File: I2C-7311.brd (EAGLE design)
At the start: 106 x 100 mm, 47 parts, among them IC1 MAX7311, J1 CONNECTOR-I2CLEFT, J2 CONNECTOR-I2CLEFT, J5 CONNECTOR-GROVE-4P-2.0-347013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, J8 CONNECTOR-GROVE-4P-2.0-347013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, SW1 A0, SW2 A1, SW3 A2

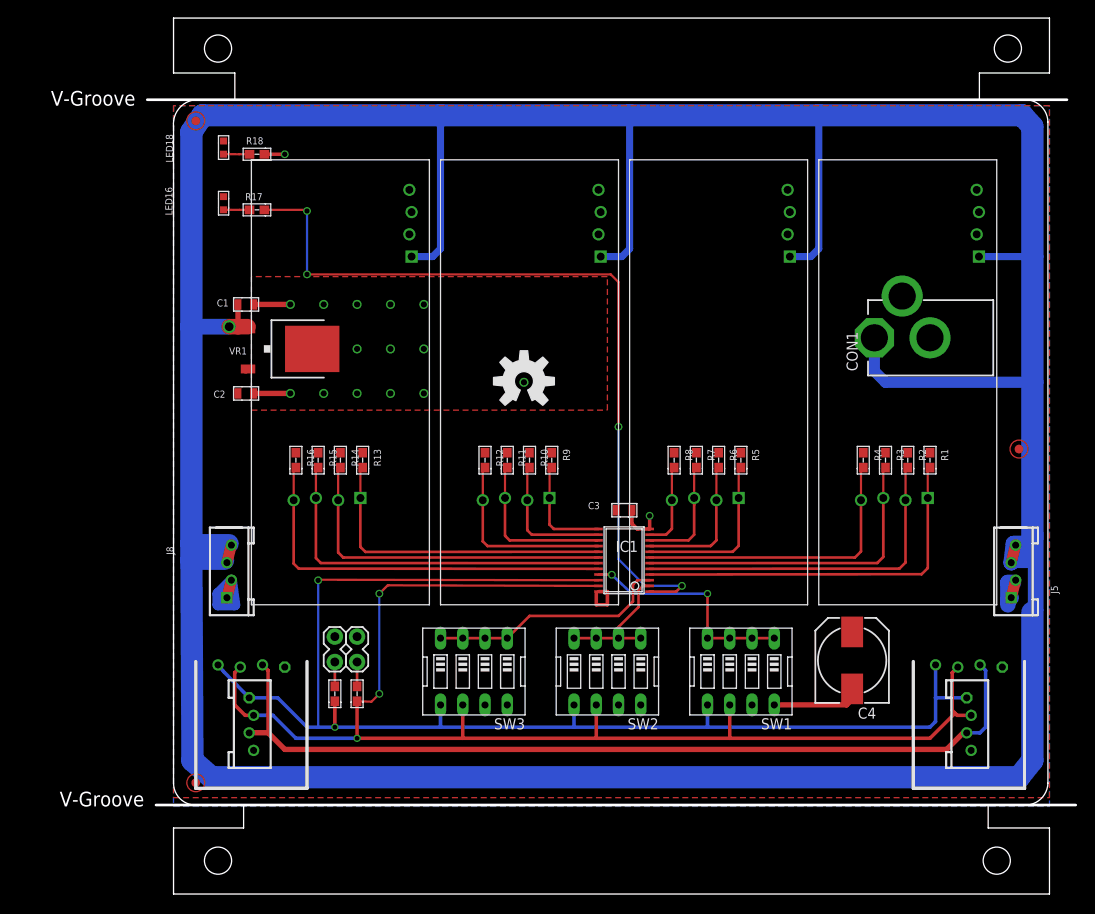
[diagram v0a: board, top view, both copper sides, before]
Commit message: 3.0 - new IOB design
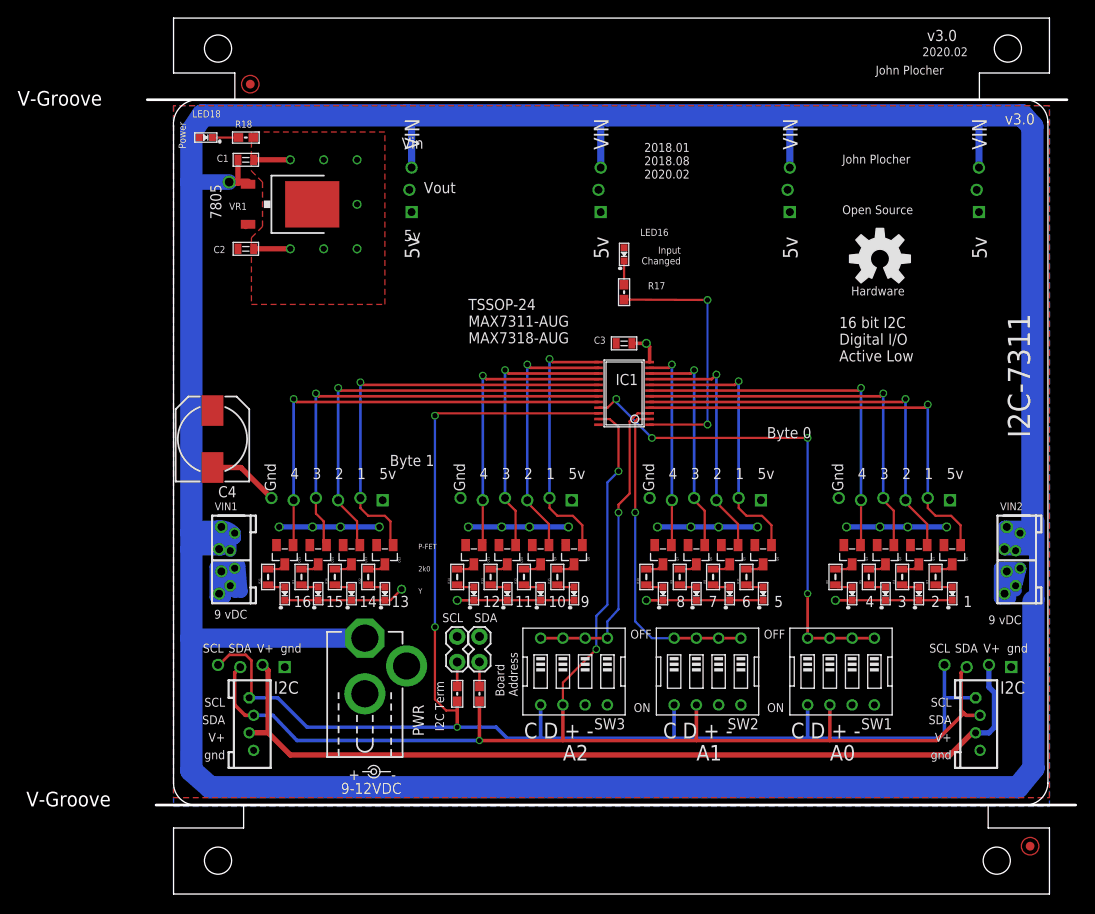
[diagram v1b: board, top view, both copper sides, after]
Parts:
- removed CON1: (no value), SPCoast:DCJ0202
- removed FID3: FIDUCIAL, SPCoast:FIDUCIAL_1MM
- removed J5, J8: CONNECTOR-GROVE-4P-2.0-3470130P1, SPCoast:4P-2.0
- removed R2, R3: 10k, SPCoast:0603-RES
- added LED1, LED10, LED11, LED12, LED13, LED14, LED15, LED17, LED2, LED3, LED4, LED5, LED6, LED7, LED8, LED9: Y, SPCoast:0603-LED
- added PWR: (no value), SPCoast:DCJ0202
- added Q0, Q1, Q10, Q11, Q12, Q13, Q14, Q15, Q2, Q3, Q4, Q5, Q6, Q7, Q8, Q9: P-FET, SPCoast:SOT23
- added R21, R22: 2K0, SPCoast:0805-RES
- added VIN: 9-12VDC, SPCoast:PWR_LABEL
- added VIN1, VIN2: CONNECTOR-POWER-L, SPCoast:POWER-R2
- BOARD1: value (none) -> BOARD80X100-IOB; device SPCoast:BOARD-DINRAIL-3.17IN-NOHOLES -> SPCoast:BOARD-DINRAIL-3.17IN-IOB
- IOB1, IOB2, IOB3, IOB4: value IO4-IOBBARE -> CONNECTOR-IO4-IOBBARE
- J1, J2: value CONNECTOR-I2CLEFT -> (none)
- R1, R10, R11, R12, R13, R14, R15, R16, R4, R5, R6, R7, R8, R9: value 10k -> 2K0; device SPCoast:0603-RES -> SPCoast:0805-RES
- SW1, SW2, SW3: device special:EDG-04 -> SPCoast:EDG-04
- moved FID2 95.5 mm to (97.8, 5.46)
- moved C4 77.3 mm to (4.45, 51.9)
- moved R1 73.0 mm to (14.6, 36.2), turned to 90 degrees
- moved LED16 46.1 mm to (51.4, 73.0)
- moved U$1 43.0 mm to (80.6, 72.5)
- moved R17 43.0 mm to (51.4, 68.7), turned to 270 degrees
- moved R7 30.4 mm to (87.0, 36.2), turned to 90 degrees
- moved R15 30.4 mm to (43.8, 36.2), turned to 90 degrees
- moved R11 30.4 mm to (65.4, 36.2), turned to 90 degrees
- moved R13 19.8 mm to (36.2, 36.2), turned to 90 degrees
- moved R5 19.8 mm to (79.4, 36.2), turned to 90 degrees
- moved R9 19.8 mm to (57.8, 36.2), turned to 90 degrees
- moved C3 19.1 mm to (51.4, 62.9)
- moved IC1 19.0 mm to (51.4, 57.1)
- moved R10 18.9 mm to (54.0, 36.2), turned to 90 degrees
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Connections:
- new net N$10: Q8.3, R15.2
- new net N$11: Q9.3, R12.2
- new net N$12: Q10.3, R13.2
- new net N$13: Q11.3, R14.2
- new net N$14: LED12.A, R15.1
- new net N$15: LED9.A, R12.1
- new net N$2: Q4.3, R11.2
- new net N$23: LED10.A, R13.1
- new net N$24: LED11.A, R14.1
- new net N$28: Q12.3, R22.2
- new net N$29: Q13.3, R16.2
- new net N$3: Q5.3, R8.2
- new net N$30: Q14.3, R1.2
- new net N$31: Q15.3, R21.2
- new net N$32: LED17.A, R22.1
- new net N$33: LED13.A, R16.1
- new net N$34: LED14.A, R1.1
- new net N$35: LED15.A, R21.1
- new net N$4: Q6.3, R9.2
- new net N$44: Q0.3, R7.2
- new net N$45: Q1.3, R4.2
- new net N$46: Q2.3, R5.2
- new net N$47: Q3.3, R6.2
- new net N$48: LED1.A, R7.1
- new net N$49: LED2.A, R4.1
- new net N$5: Q7.3, R10.2
- new net N$50: LED3.A, R5.1
- new net N$51: LED4.A, R6.1
- new net N$6: LED8.A, R11.1
- new net N$7: LED5.A, R8.1
- new net N$8: LED6.A, R9.1
- new net N$9: LED7.A, R10.1
- net +9V: now also PWR.1, VIN1.V+, VIN1.V+@1, VIN1.V+@2, VIN1.V+@3, VIN2.V+, VIN2.V+@1, VIN2.V+@2, VIN2.V+@3; no longer CON1.1, J5.3, J5.4, J8.3, J8.4
- net GND: now also IOB1.G@3, IOB2.G@3, IOB3.G@3, IOB4.G@3, LED1.C, LED10.C, LED11.C, LED12.C, LED13.C, LED14.C, LED15.C, LED17.C, LED2.C, LED3.C, LED4.C, LED5.C, LED6.C, LED7.C, LED8.C, LED9.C, PWR.2, PWR.3, VIN1.GND, VIN1.GND@1, VIN1.GND@2, VIN1.GND@3, VIN2.GND, VIN2.GND@1, VIN2.GND@2, VIN2.GND@3; no longer CON1.2, CON1.3, IOB1.G@1, IOB1.G@2, IOB2.G@1, IOB2.G@2, IOB3.G@1, IOB3.G@2, IOB4.G@1, IOB4.G@2, J5.1, J5.2, J8.1, J8.2
- net P1: now also Q0.1; no longer R1.2
- net P10: now also Q9.1; no longer R10.2
- net P11: now also Q10.1; no longer R11.2
- net P12: now also Q11.1; no longer R12.2
- net P13: now also Q12.1; no longer R13.2
- net P14: now also Q13.1; no longer R14.2
- net P15: now also Q14.1; no longer R15.2
- net P16: now also Q15.1; no longer R16.2
- net P2: now also Q1.1; no longer R2.2
- net P3: now also Q2.1; no longer R3.2
- net P4: now also Q3.1; no longer R4.2
- net P5: now also Q4.1; no longer R5.2
- net P6: now also Q5.1; no longer R6.2
- net P7: now also Q6.1; no longer R7.2
- net P8: now also Q7.1; no longer R8.2
- net P9: now also Q8.1; no longer R9.2
- net VCC: now also IOB1.V5@1, IOB2.V5@1, IOB3.V5@1, IOB4.V5@1, Q0.2, Q1.2, Q10.2, Q11.2, Q12.2, Q13.2, Q14.2, Q15.2, Q2.2, Q3.2, Q4.2, Q5.2, Q6.2, Q7.2, Q8.2, Q9.2; no longer R1.1, R10.1, R11.1, R12.1, R13.1, R14.1, R15.1, R16.1, R2.1, R3.1, R4.1, R5.1, R6.1, R7.1, R8.1, R9.1
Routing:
- net GND: track 42.1 -> 112.2 mm, vias 16 -> 12
- net !INT: track 92.2 -> 30.4 mm, vias 4 -> 2
- net VCC: track 5.42 -> 50.9 mm, vias 0 -> 16
- net A0: track 26.0 -> 56.8 mm, vias 2 -> 4
- net A1: track 15.5 -> 37.9 mm, vias 0 -> 1
- net +9V: track 455.8 -> 436.4 mm
- net P9: track 12.4 -> 29.6 mm, vias 0 -> 1
- net SCL: track 154.6 -> 170.5 mm, vias 2 -> 3
- net P10: track 15.6 -> 29.9 mm, vias 0 -> 1
- net P8: track 9.90 -> 23.6 mm, vias 0 -> 1
- net P11: track 18.8 -> 31.3 mm, vias 0 -> 1
- net P5: track 19.5 -> 31.6 mm, vias 0 -> 1
- net P7: track 13.9 -> 25.7 mm, vias 0 -> 1
- net P6: track 16.8 -> 28.3 mm, vias 0 -> 1
- net P13: track 36.6 -> 48.1 mm, vias 0 -> 1
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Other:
- board text added: "1"
- board text added: "10"
- board text added: "11"
- board text added: "12"
- board text added: "13"
- board text added: "14"
- board text added: "15"
- board text added: "16"
- board text added: "2"
- board text added: "2018.01 2018.08 2020.02"
- board text added: "2020.02"
- board text added: "2k0"
- board text added: "3"
- board text added: "3.0 - new IOB footprint"
- board text added: "4"
- board text added: "5"
- board text added: "6"
- board text added: "7"
- board text added: "8"
- board text added: "9"
- board text added: "OFF"
- board text added: "ON"
- board text added: "P-FET"
- board text added: "TSSOP-24 MAX7311-AUG MAX7318-AUG"
- board text added: "Vout"
- board text added: "Y"
- board text added: "v3.0"
- board text removed: "10k pullups for use with MAX7312"
- board text removed: "2018.01 2018.08"
- board text removed: "2018.08"
- board text removed: "4 3 2 1"
- board text removed: "8 7 6 5"
- board text removed: "External daughterboards for each IO bank Eliminates having to custom cut 3M track Eliminates having to stock signal driver I2C boards Custom input low pass filters can be added to Detector and Turtle drivers 2.0 - fixed footprint for U1, DB keepout violations 2.1 - Added carrier template, optional DC barrel power jack"
- board text removed: "I2C-7311-IO"
- board text removed: "MAX7311 /12 AUG or PCA9675PW"
- board text removed: "gnd"
- board text removed: "v2.1"

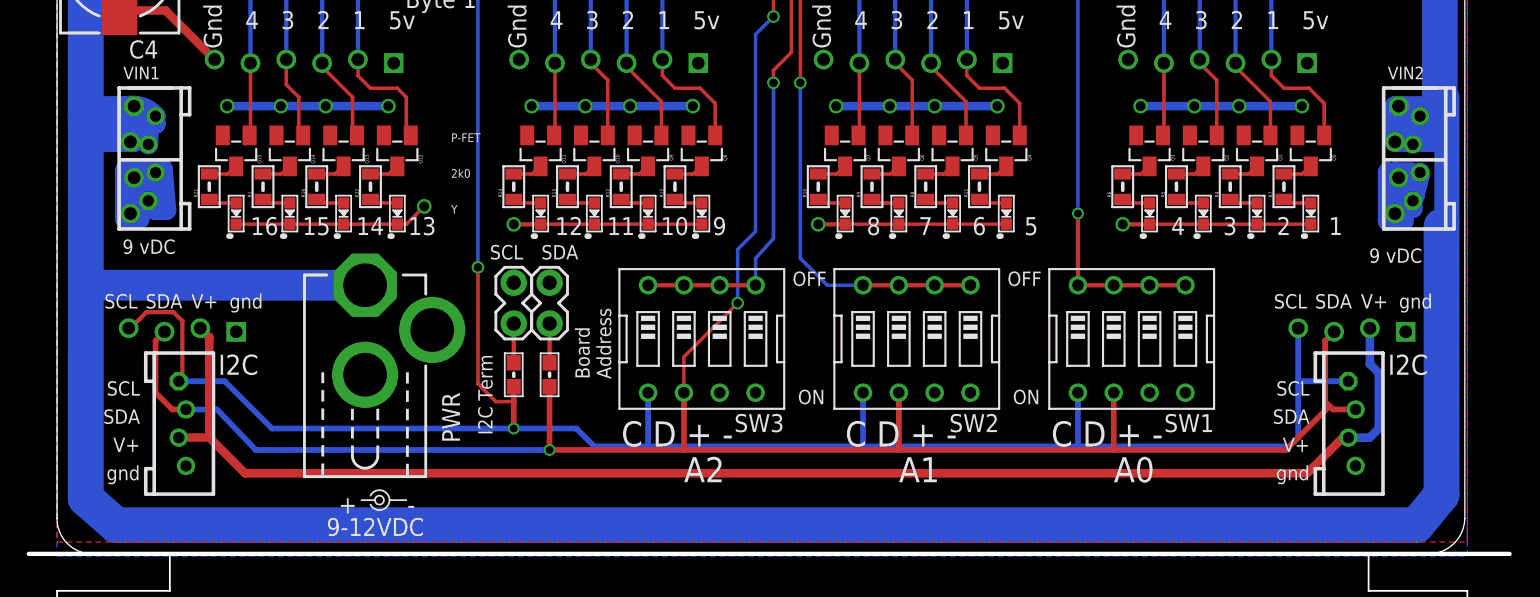
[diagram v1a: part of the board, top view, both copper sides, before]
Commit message: updated SPCoast lib for IO4-IOB silkscreen
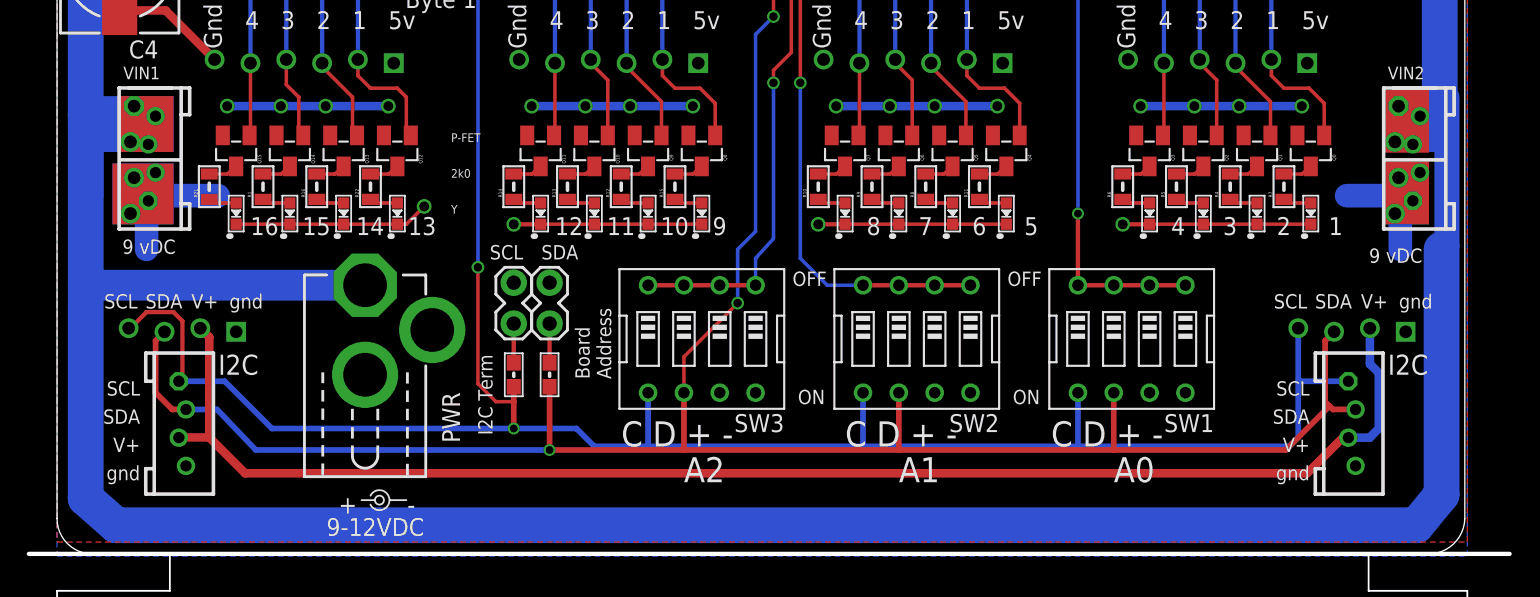
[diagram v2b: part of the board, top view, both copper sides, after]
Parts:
- IOB1, IOB2, IOB3: value CONNECTOR-IO4-IOBBARE -> CONNECTOR-IO4-IOBCLEAN; device SPCoast:IO4-IOB -> SPCoast:IOB-IO4-CLEAN
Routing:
- net GND: track 112.2 -> 100.2 mm
- net +9V: track 436.4 -> 429.3 mm
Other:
- board text removed: "Made in the PCR, Coast Division, NMRA"
- board text removed: "Model Railroading is fun!"

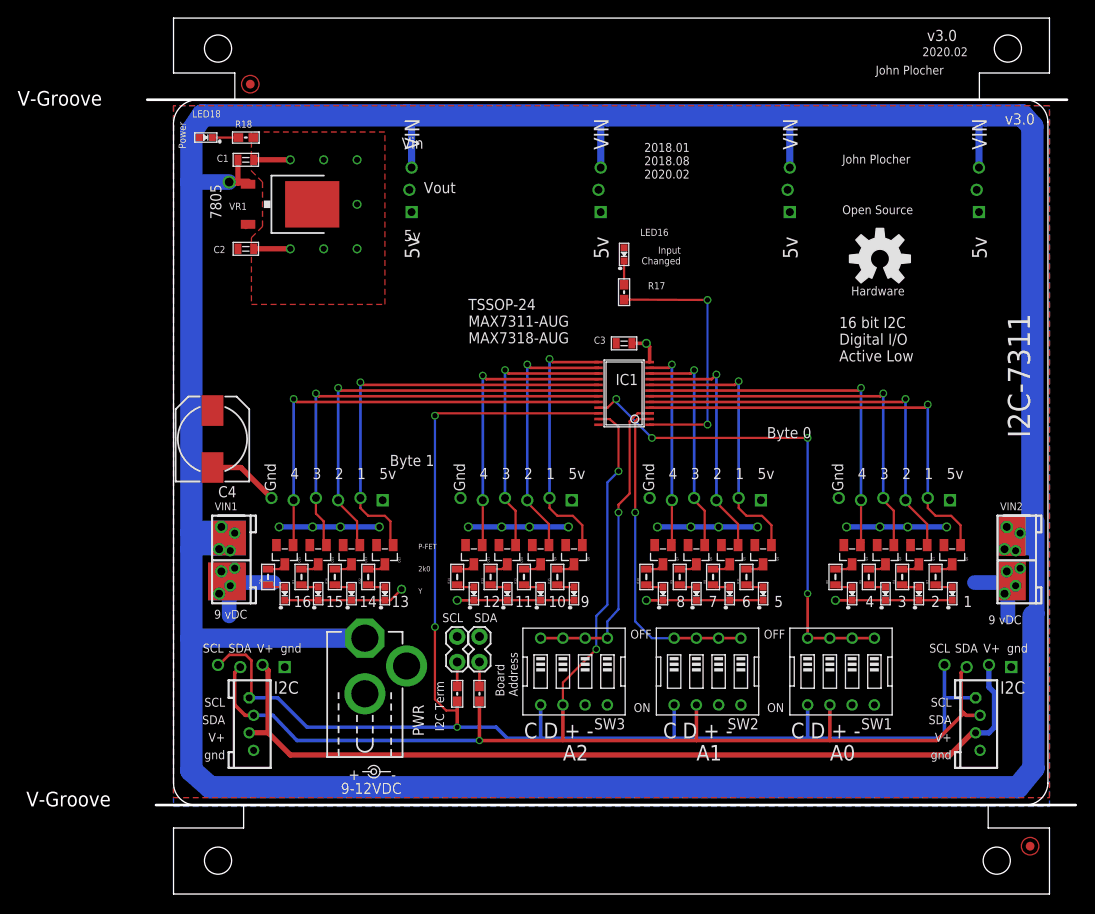
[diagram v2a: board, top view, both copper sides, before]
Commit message: updated SPCoast.lbr: LED, VR, C-POL to match reel orientation
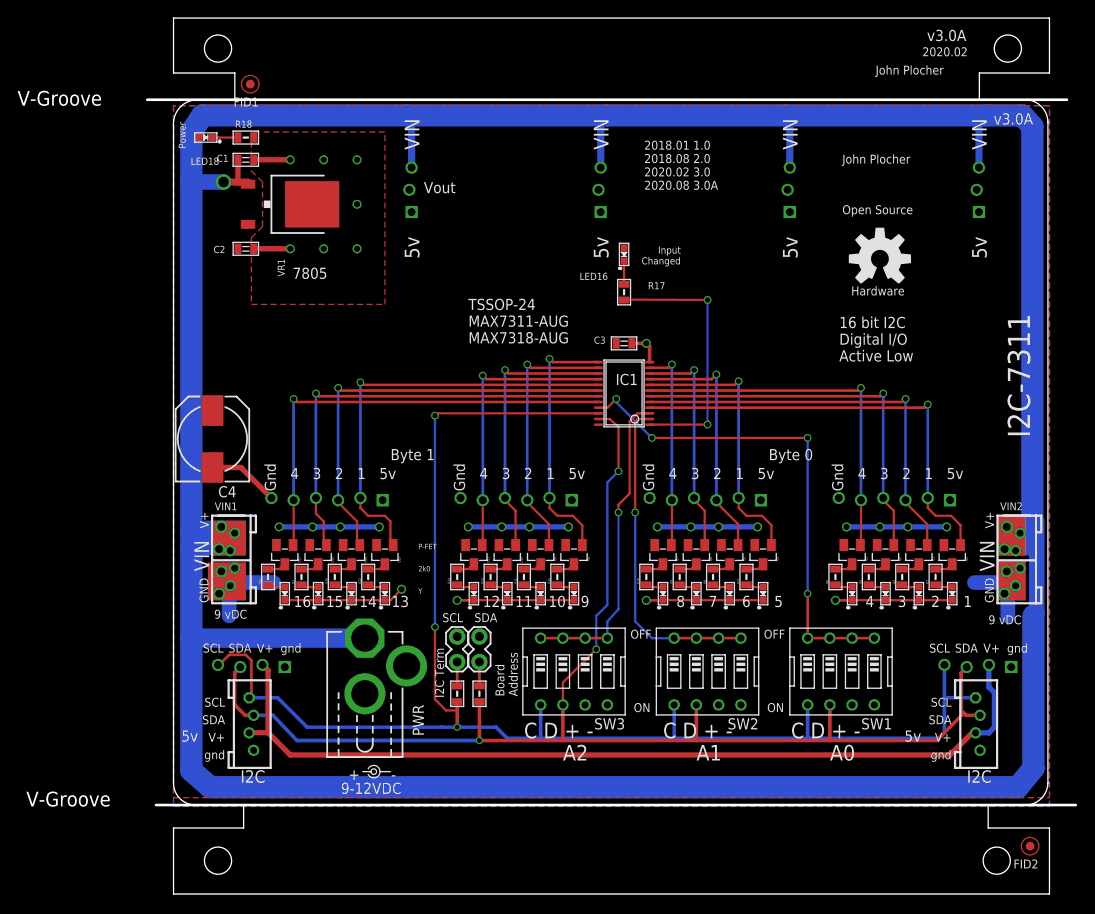
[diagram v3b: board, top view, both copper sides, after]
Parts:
- LED16, LED18: value DIM-GREEN -> G
- R17: value 2k2 -> 2k0; device SPCoast:0603-RES -> SPCoast:0805-RES
- R18: value 2K2 -> 2K0; device SPCoast:0603-RES -> SPCoast:0805-RES
- R19, R20: device SPCoast:0603-RES -> SPCoast:0805-RES
- turned LED1 to 90 degrees
- turned LED10 to 90 degrees
- turned LED11 to 90 degrees
- turned LED12 to 90 degrees
- turned LED13 to 90 degrees
- turned LED14 to 90 degrees
- turned LED15 to 90 degrees
- turned LED16 to 90 degrees
- turned LED17 to 90 degrees
- turned LED18 to 180 degrees
- turned LED2 to 90 degrees
- turned LED3 to 90 degrees
- turned LED4 to 90 degrees
- turned LED5 to 90 degrees
- turned LED6 to 90 degrees
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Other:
- board text added: "2018.01 1.0 2018.08 2.0 2020.02 3.0 2020.08 3.0A"
- board text added: "3.0A - Fixed C-POL, LED and VREG library component orientations to match default reel orientation, no PCB changes"
- board text added: "A "1" bit in the I/O register is associated with a LOW voltage on a pin, and a LIT feedback LED."
- board text added: "v3.0A"
- board text removed: "2018.01 2018.08 2020.02"
- board text removed: "3.0 - new IOB footprint"
- board text removed: "A "1" bit in the I/O register is associated with a LOW voltage on a pin"
- board text removed: "Vin"
- board text removed: "v3.0"

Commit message: V3.1
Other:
- board text added: "2020.08"
- board text added: "v3.1"
- board text removed: "2020.02"
- board text removed: "v3.0A"
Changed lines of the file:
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@@
 <board>
 <plain>
-<text x="93.63339375" y="87.855534375" size="1.27" layer="21" rot="SR0">v3.0A</text>
+<text x="93.63339375" y="87.855534375" size="1.27" layer="21" rot="SR0">v3.1</text>
 <text x="81.9564" y="18.4404" size="1.778" layer="22" ratio="10" rot="SMR0">Active Low:</text>
 <text x="2.2548" y="40.2418" size="1.4224" layer="22" font="vector" ratio="15" rot="MR270">www. SP Coast .com</text>
@@
 <text x="67.945" y="49.53" size="1.27" layer="21" rot="SR0">Byte 0</text>
 <text x="24.765" y="49.53" size="1.27" layer="21" rot="SR0">Byte 1</text>
-<text x="86.01339375" y="97.380534375" size="1.27" layer="21" rot="SR0">v3.0A</text>
-<text x="85.48799375" y="95.645009375" size="1.016" layer="21">2020.02</text>
+<text x="86.01339375" y="97.380534375" size="1.27" layer="21" rot="SR0">v3.1</text>
+<text x="85.48799375" y="95.645009375" size="1.016" layer="21">2020.08</text>
 <text x="53.73799375" y="80.405009375" size="1.016" layer="21">2018.01 1.0
 2018.08 2.0
